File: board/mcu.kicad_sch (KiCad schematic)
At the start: 1 part, among them U8 STM32G0B0CETx

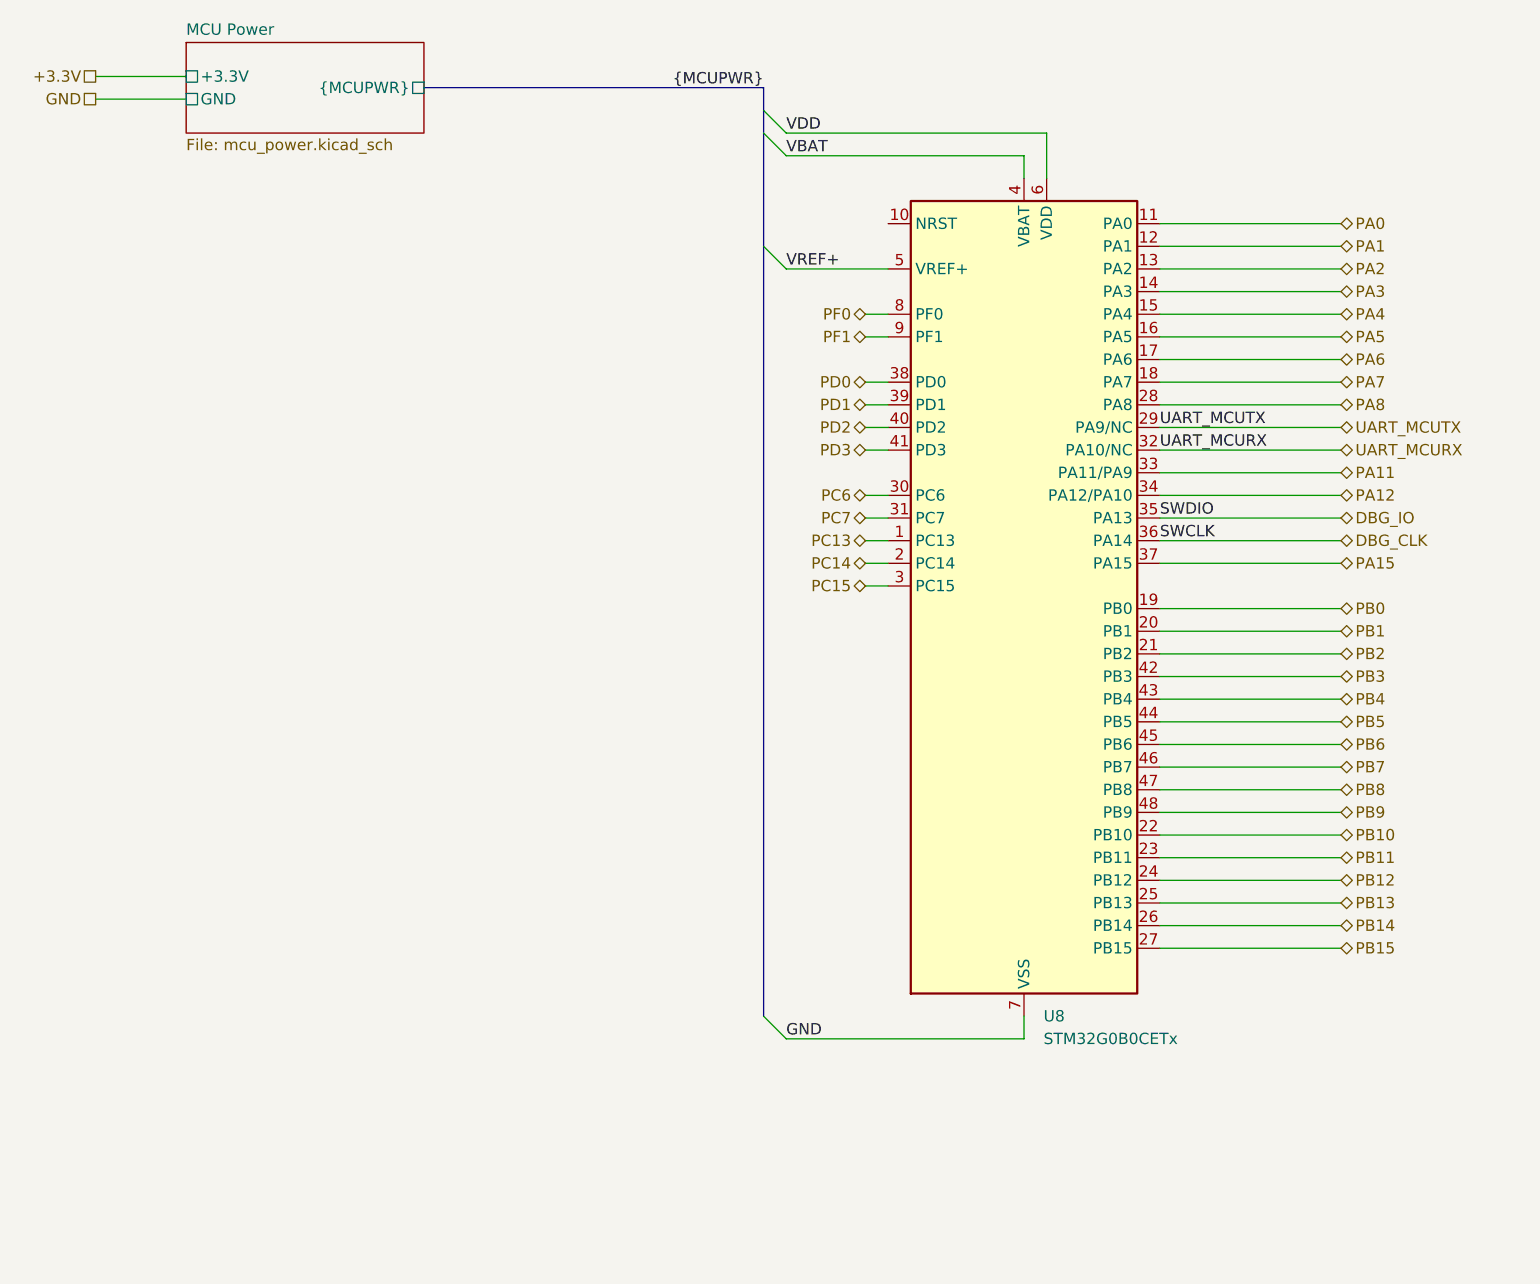
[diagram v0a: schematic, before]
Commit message: initial board layout (WIP), schematic tuning
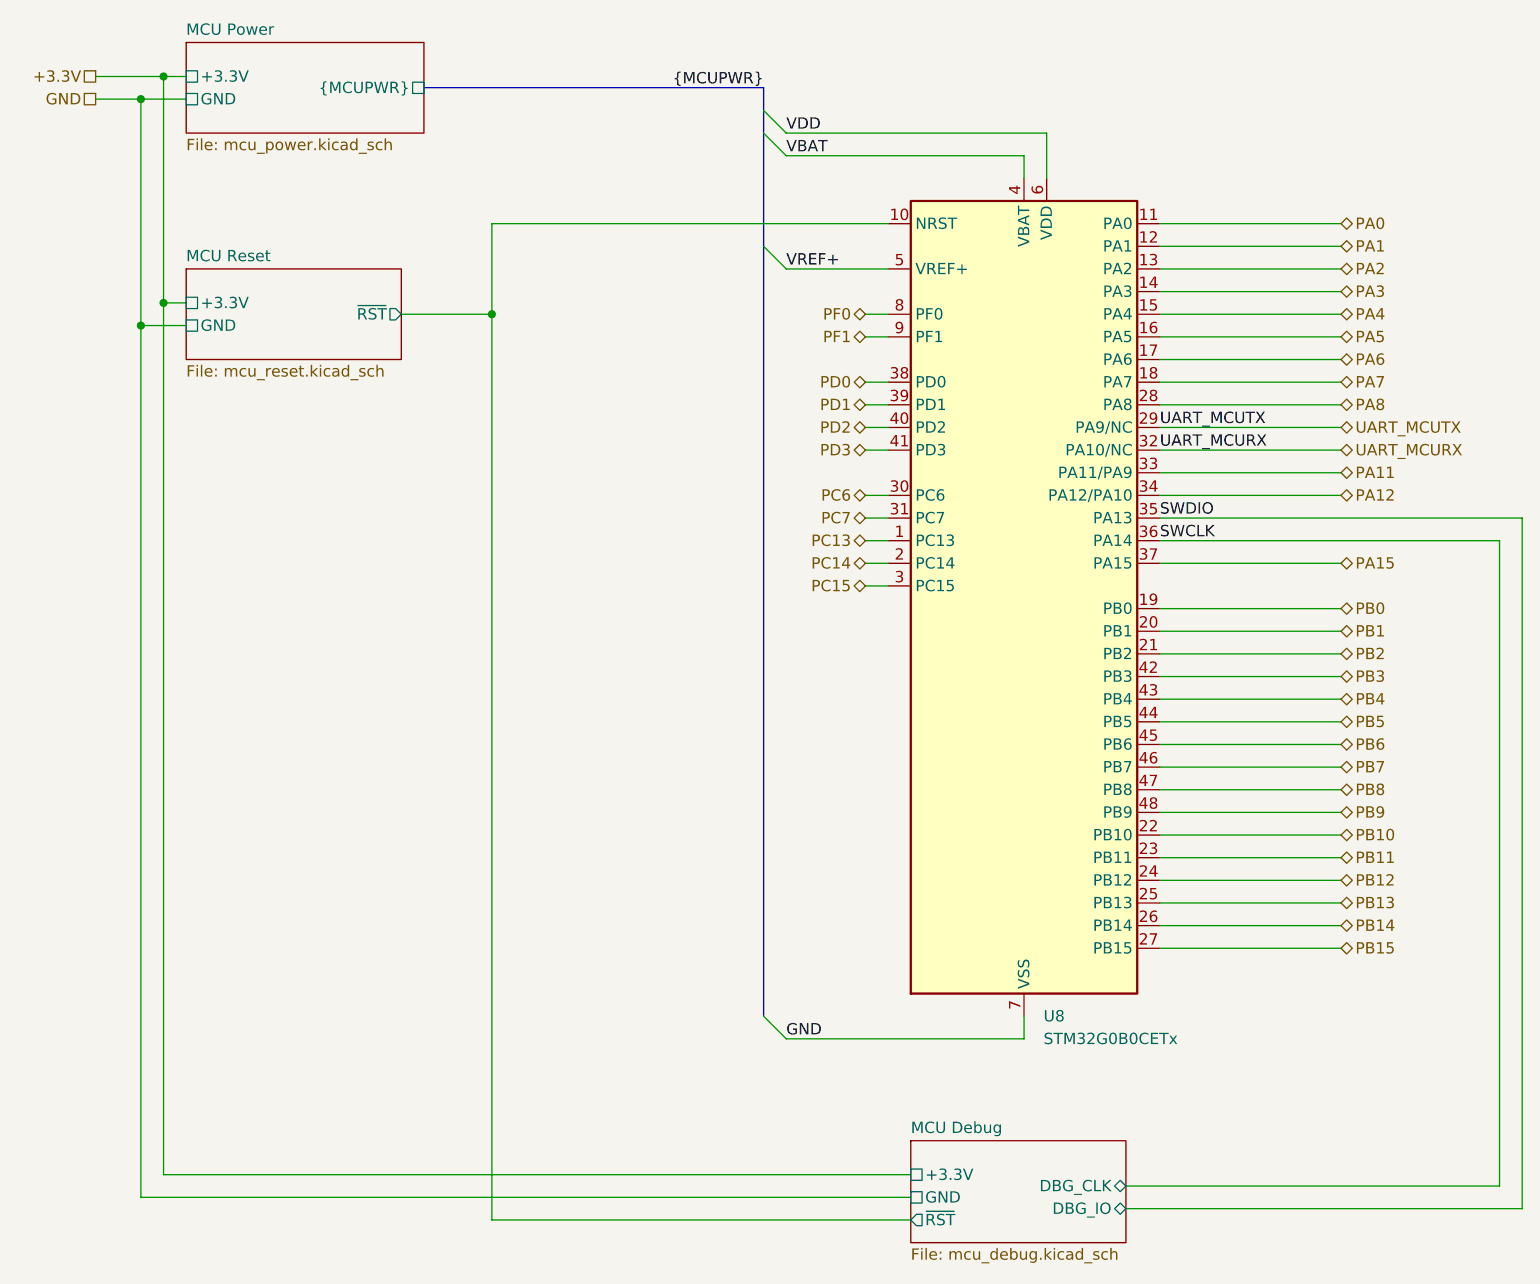
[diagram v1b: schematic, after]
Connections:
- net MCU Debug/~{RST}: now reaches U8.10 (NRST)
- net DBG_CLK renamed SWCLK
- net DBG_IO renamed SWDIO
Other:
- added sheet MCU Debug (mcu_debug.kicad_sch)
- added sheet MCU Reset (mcu_reset.kicad_sch)
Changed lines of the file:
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@@
 (kicad_sch (version 20230121) (generator eeschema)
   (paper "A4")
+  (junction (at 38.1 66.04) (diameter 0) (color 0 0 0 0)
+  )
+  (junction (at 40.64 38.1) (diameter 0) (color 0 0 0 0)
+  )
+  (junction (at 40.64 63.5) (diameter 0) (color 0 0 0 0)
+  )
+  (junction (at 77.47 64.77) (diameter 0) (color 0 0 0 0)
+  )
+  (junction (at 38.1 40.64) (diameter 0) (color 0 0 0 0)
+  )
   (bus_entry (at 107.95 143.51) (size 2.54 2.54)
     (stroke (width 0) (type default))
@@
     (stroke (width 0) (type default))
   )
+  (wire (pts (xy 77.47 166.37) (xy 124.46 166.37))
+    (stroke (width 0) (type default))
+  )
   (wire (pts (xy 119.38 77.47) (xy 121.92 77.47))
     (stroke (width 0) (type default))
   )
+  (wire (pts (xy 77.47 54.61) (xy 121.92 54.61))
+    (stroke (width 0) (type default))
+  )
   (bus (pts (xy 107.95 44.45) (xy 107.95 41.91))
     (stroke (width 0) (type default))
@@
     (stroke (width 0) (type default))
   )
-  (wire (pts (xy 152.4 87.63) (xy 172.72 87.63))
+  (wire (pts (xy 152.4 87.63) (xy 193.04 87.63))
+    (stroke (width 0) (type default))
+  )
+  (wire (pts (xy 38.1 163.83) (xy 124.46 163.83))
     (stroke (width 0) (type default))
   )
@@
     (stroke (width 0) (type default))
   )
+  (wire (pts (xy 38.1 40.64) (xy 43.18 40.64))
+    (stroke (width 0) (type default))
+  )
   (wire (pts (xy 172.72 115.57) (xy 152.4 115.57))
     (stroke (width 0) (type default))
   )
+  (wire (pts (xy 67.31 64.77) (xy 77.47 64.77))
+    (stroke (width 0) (type default))
+  )
   (wire (pts (xy 172.72 62.23) (xy 152.4 62.23))
     (stroke (width 0) (type default))
   )
+  (wire (pts (xy 40.64 38.1) (xy 43.18 38.1))
+    (stroke (width 0) (type default))
+  )
+  (wire (pts (xy 40.64 161.29) (xy 124.46 161.29))
+    (stroke (width 0) (type default))
+  )
   (wire (pts (xy 172.72 82.55) (xy 152.4 82.55))
     (stroke (width 0) (type default))
@@
     (stroke (width 0) (type default))
   )
-  (wire (pts (xy 152.4 90.17) (xy 172.72 90.17))
+  (wire (pts (xy 40.64 63.5) (xy 40.64 161.29))
+    (stroke (width 0) (type default))
+  )
+  (wire (pts (xy 33.02 38.1) (xy 40.64 38.1))
+    (stroke (width 0) (type default))
+  )
+  (wire (pts (xy 152.4 90.17) (xy 190.5 90.17))
     (stroke (width 0) (type default))
   )
@@
     (stroke (width 0) (type default))
   )
+  (wire (pts (xy 77.47 64.77) (xy 77.47 166.37))
+    (stroke (width 0) (type default))
+  )
+  (wire (pts (xy 193.04 165.1) (xy 193.04 87.63))
+    (stroke (width 0) (type default))
+  )
   (wire (pts (xy 172.72 133.35) (xy 152.4 133.35))
     (stroke (width 0) (type default))
@@
     (stroke (width 0) (type default))
   )
-  (wire (pts (xy 33.02 38.1) (xy 43.18 38.1))
-    (stroke (width 0) (type default))
-  )
   (wire (pts (xy 172.72 54.61) (xy 152.4 54.61))
     (stroke (width 0) (type default))
@@
     (stroke (width 0) (type default))
   )
-  (wire (pts (xy 33.02 40.64) (xy 43.18 40.64))
+  (wire (pts (xy 33.02 40.64) (xy 38.1 40.64))
     (stroke (width 0) (type default))
   )
@@
     (stroke (width 0) (type default))
   )
+  (wire (pts (xy 190.5 162.56) (xy 190.5 90.17))
+    (stroke (width 0) (type default))
+  )
   (wire (pts (xy 119.38 72.39) (xy 121.92 72.39))
     (stroke (width 0) (type default))
@@
     (stroke (width 0) (type default))
   )
+  (wire (pts (xy 38.1 40.64) (xy 38.1 66.04))
+    (stroke (width 0) (type default))
+  )
+  (wire (pts (xy 38.1 66.04) (xy 38.1 163.83))
+    (stroke (width 0) (type default))
+  )
   (wire (pts (xy 110.49 59.69) (xy 121.92 59.69))
     (stroke (width 0) (type default))
@@
     (stroke (width 0) (type default))
   )
+  (wire (pts (xy 40.64 38.1) (xy 40.64 63.5))
+    (stroke (width 0) (type default))
+  )
   (wire (pts (xy 119.38 90.17) (xy 121.92 90.17))
     (stroke (width 0) (type default))
@@
     (stroke (width 0) (type default))
   )
+  (wire (pts (xy 38.1 66.04) (xy 43.18 66.04))
+    (stroke (width 0) (type default))
+  )
   (wire (pts (xy 110.49 44.45) (xy 139.7 44.45))
     (stroke (width 0) (type default))
@@
     (stroke (width 0) (type default))
   )
+  (wire (pts (xy 77.47 54.61) (xy 77.47 64.77))
+    (stroke (width 0) (type default))
+  )
+  (wire (pts (xy 148.59 162.56) (xy 190.5 162.56))
+    (stroke (width 0) (type default))
+  )
   (wire (pts (xy 137.16 46.99) (xy 137.16 49.53))
     (stroke (width 0) (type default))
   )
+  (wire (pts (xy 148.59 165.1) (xy 193.04 165.1))
+    (stroke (width 0) (type default))
+  )
   (wire (pts (xy 172.72 67.31) (xy 152.4 67.31))
     (stroke (width 0) (type default))
@@
   )
   (wire (pts (xy 152.4 77.47) (xy 172.72 77.47))
+    (stroke (width 0) (type default))
+  )
+  (wire (pts (xy 40.64 63.5) (xy 43.18 63.5))
     (stroke (width 0) (type default))
   )
@@
     (effects (font (size 1.27 1.27)) (justify left))
   )
-  (hierarchical_label "DBG_IO" (shape bidirectional) (at 172.72 87.63 0) (fields_autoplaced)
-    (effects (font (size 1.27 1.27)) (justify left))
-  )
   (hierarchical_label "PA0" (shape bidirectional) (at 172.72 54.61 0) (fields_autoplaced)
     (effects (font (size 1.27 1.27)) (justify left))
@@
   )
   (hierarchical_label "PB12" (shape bidirectional) (at 172.72 128.27 0) (fields_autoplaced)
-    (effects (font (size 1.27 1.27)) (justify left))
-  )
-  (hierarchical_label "DBG_CLK" (shape bidirectional) (at 172.72 90.17 0) (fields_autoplaced)
     (effects (font (size 1.27 1.27)) (justify left))
   )
@@
       (effects (font (size 1.27 1.27)) hide)
     )
+    (pin "1")
+    (pin "10")
     (pin "11")
+    (pin "12")
+    (pin "13")
+    (pin "14")
+    (pin "15")
+    (pin "16")
+    (pin "17")
+    (pin "18")
+    (pin "19")
+    (pin "2")
+    (pin "20")
+    (pin "21")
+    (pin "22")
+    (pin "23")
+    (pin "24")
+    (pin "25")
+    (pin "26")
+    (pin "27")
+    (pin "28")
+    (pin "29")
+    (pin "3")
+    (pin "30")
     (pin "31")
+    (pin "32")
+    (pin "33")
+    (pin "34")
+    (pin "35")
+    (pin "36")
     (pin "37")
-    (pin "24")
-    (pin "29")
-    (pin "7")
-    (pin "27")
-    (pin "47")
-    (pin "17")
-    (pin "15")
-    (pin "32")
-    (pin "19")
-    (pin "25")
-    (pin "33")
     (pin "38")
-    (pin "42")
-    (pin "36")
-    (pin "45")
-    (pin "8")
-    (pin "13")
+    (pin "39")
+    (pin "4")
     (pin "40")
     (pin "41")
-    (pin "2")
-    (pin "12")
+    (pin "42")
     (pin "43")
-    (pin "6")
-    (pin "30")
-    (pin "9")
-    (pin "23")
-    (pin "18")
+    (pin "44")
+    (pin "45")
+    (pin "46")
+    (pin "47")
     (pin "48")
     (pin "5")
-    (pin "44")
-    (pin "1")
-    (pin "14")
-    (pin "20")
-    (pin "28")
-    (pin "39")
-    (pin "16")
-    (pin "22")
-    (pin "21")
-    (pin "3")
-    (pin "34")
-    (pin "4")
-    (pin "26")
-    (pin "10")
-    (pin "46")
-    (pin "35")
+    (pin "6")
+    (pin "7")
+    (pin "8")
+    (pin "9")
     (instances
       (project "eprom5vread"
@@
       )
     )
+  )
+  (sheet (at 124.46 157.48) (size 24.13 11.43) (fields_autoplaced)
+    (stroke (width 0.1524) (type solid))
+    (fill (color 0 0 0 0.0000))
+    (property "Sheetname" "MCU Debug" (at 124.46 156.7684 0)
+      (effects (font (size 1.27 1.27)) (justify left bottom))
+    )
+    (property "Sheetfile" "mcu_debug.kicad_sch" (at 124.46 169.4946 0)
+      (effects (font (size 1.27 1.27)) (justify left top))
+    )
+    (pin "DBG_IO" bidirectional (at 148.59 165.1 0)
+      (effects (font (size 1.27 1.27)) (justify right))
+    )
+    (pin "DBG_CLK" bidirectional (at 148.59 162.56 0)
+      (effects (font (size 1.27 1.27)) (justify right))
+    )
+    (pin "~{RST}" output (at 124.46 166.37 180)
+      (effects (font (size 1.27 1.27)) (justify left))
+    )
+    (pin "GND" passive (at 124.46 163.83 180)
+      (effects (font (size 1.27 1.27)) (justify left))
+    )
+    (pin "+3.3V" passive (at 124.46 161.29 180)
+      (effects (font (size 1.27 1.27)) (justify left))
+    )
+    (instances
+      (project "eprom5vread"
+        (path "/b08a8275-42d3-43c1-b04c-f89506e7527b/2fd5d481-fecc-449f-aabd-88adee8fd543" (page "6"))
+      )
+    )
+  )
+  (sheet (at 43.18 59.69) (size 24.13 10.16) (fields_autoplaced)
+    (stroke (width 0.1524) (type solid))
+    (fill (color 0 0 0 0.0000))
+    (property "Sheetname" "MCU Reset" (at 43.18 58.9784 0)
+      (effects (font (size 1.27 1.27)) (justify left bottom))
+    )
+    (property "Sheetfile" "mcu_reset.kicad_sch" (at 43.18 70.4346 0)
+      (effects (font (size 1.27 1.27)) (justify left top))
+    )
+    (pin "~{RST}" output (at 67.31 64.77 0)
+      (effects (font (size 1.27 1.27)) (justify right))
+    )
+    (pin "GND" passive (at 43.18 66.04 180)
+      (effects (font (size 1.27 1.27)) (justify left))
+    )
+    (pin "+3.3V" passive (at 43.18 63.5 180)
+      (effects (font (size 1.27 1.27)) (justify left))
+    )
+    (instances
+      (project "eprom5vread"
+        (path "/b08a8275-42d3-43c1-b04c-f89506e7527b/2fd5d481-fecc-449f-aabd-88adee8fd543" (page "5"))
+      )
+    )

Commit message: finish board design
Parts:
- renumbered U8 to U101
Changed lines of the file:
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@@
   (symbol (lib_id "MCU_ST_STM32G0:STM32G0B0CETx") (at 137.16 97.79 0) (unit 1)
     (in_bom yes) (on_board yes) (dnp no) (fields_autoplaced)
-    (property "Reference" "U8" (at 139.3541 143.51 0)
+    (property "Reference" "U101" (at 139.3541 143.51 0)
       (effects (font (size 1.27 1.27)) (justify left))
     )
@@
       (project "eprom5vread"
         (path "/b08a8275-42d3-43c1-b04c-f89506e7527b/2fd5d481-fecc-449f-aabd-88adee8fd543"
-          (reference "U8") (unit 1)
+          (reference "U101") (unit 1)
         )
       )
